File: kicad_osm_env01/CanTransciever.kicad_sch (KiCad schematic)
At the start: 21 parts

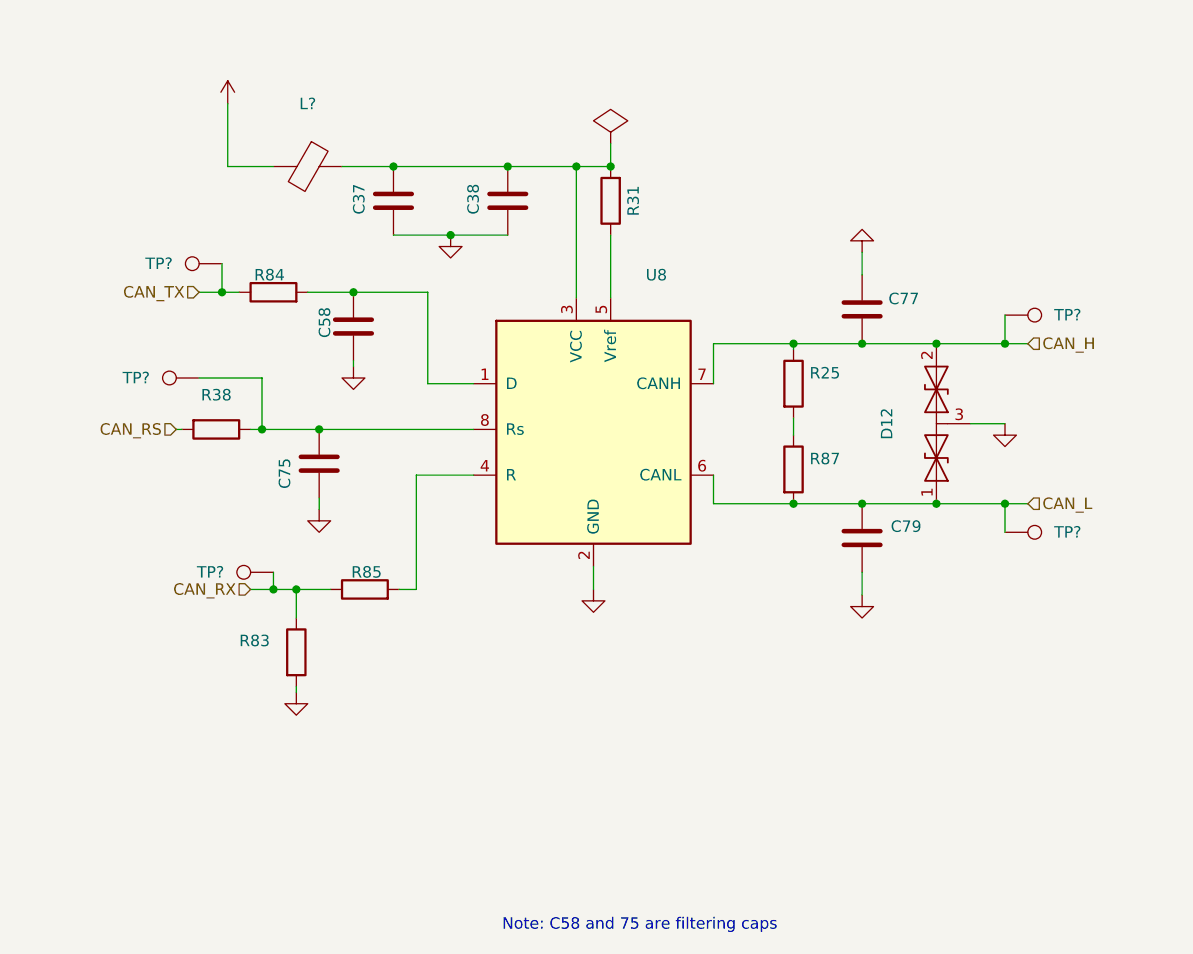
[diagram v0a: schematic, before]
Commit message: added stml433 to schematic and carried out some mods
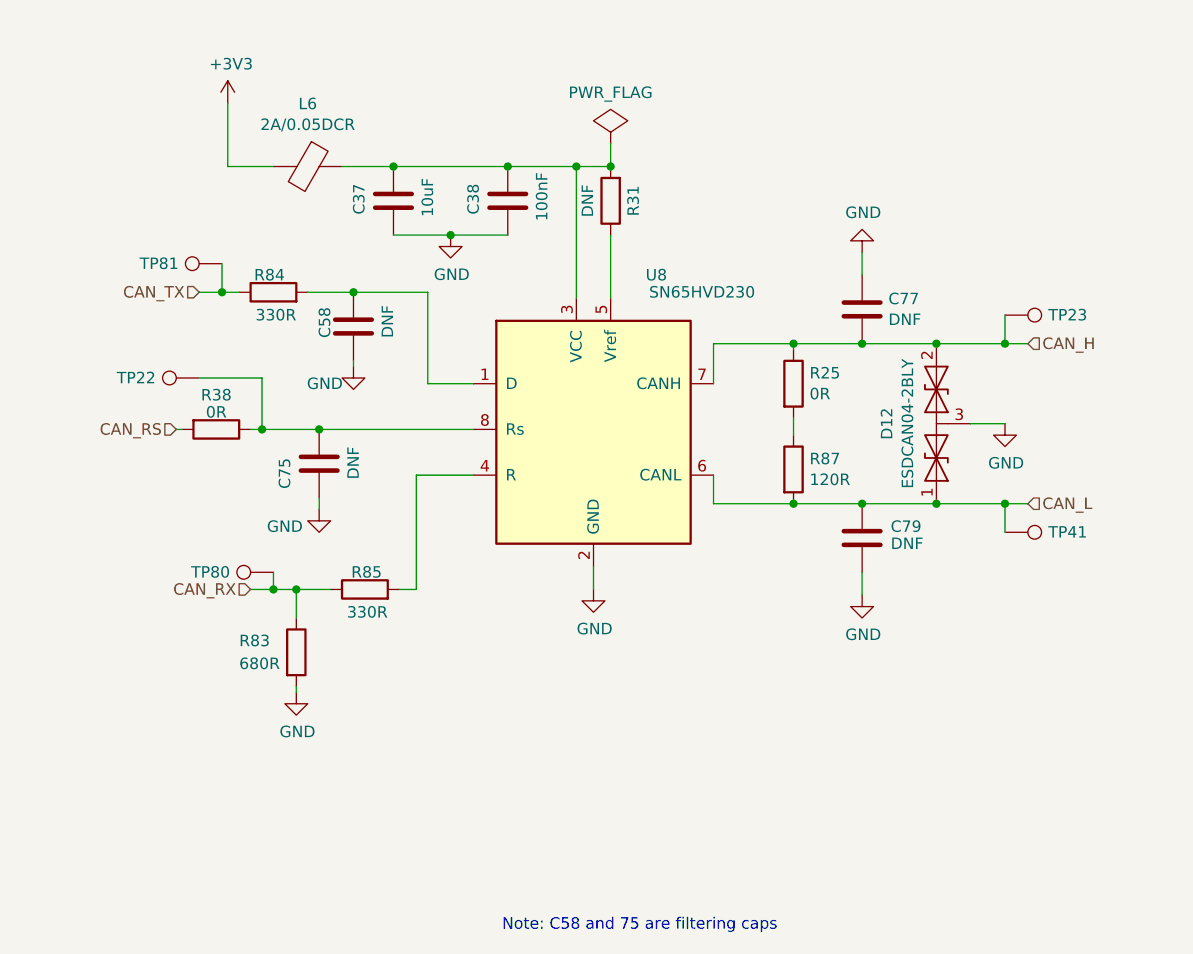
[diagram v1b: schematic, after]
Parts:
- C37: value (none) -> 10uF; footprint (none) -> Capacitor_SMD:C_0603_1608Metric
- C38: value (none) -> 100nF; footprint (none) -> Capacitor_SMD:C_0402_1005Metric
- C58, C75, C77, C79: value (none) -> DNF; footprint (none) -> Capacitor_SMD:C_0603_1608Metric
- D12: value (none) -> ESDCAN04-2BLY; footprint (none) -> Package_TO_SOT_SMD:SOT-23
- L6: renamed from L?; value (none) -> 2A/0.05DCR; footprint (none) -> Inductor_SMD:L_0402_1005Metric
- R25, R38: value (none) -> 0R; footprint (none) -> Resistor_SMD:R_0603_1608Metric
- R31: value (none) -> DNF; footprint (none) -> Resistor_SMD:R_0603_1608Metric
- R83: value (none) -> 680R; footprint (none) -> Resistor_SMD:R_0603_1608Metric
- R84, R85: value (none) -> 330R; footprint (none) -> Resistor_SMD:R_0603_1608Metric
- R87: value (none) -> 120R; footprint (none) -> Resistor_SMD:R_0603_1608Metric
- TP22, TP23, TP41, TP80, TP81: renamed from TP?; value (none) -> Test_Point; footprint (none) -> TestPoint:TestPoint_Pad_D1.5mm
- U8: value (none) -> SN65HVD230; footprint (none) -> Package_SO:SOIC-8_3.9x4.9mm_P1.27mm

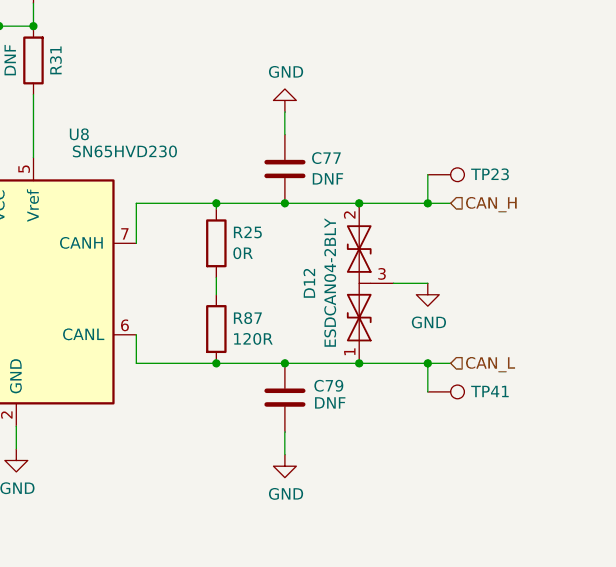
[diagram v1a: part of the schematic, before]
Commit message: updated mod list
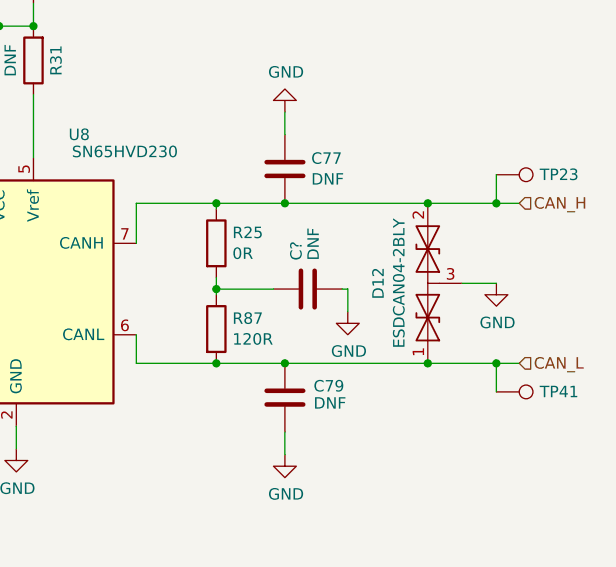
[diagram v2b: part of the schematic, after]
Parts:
- added C?: DNF, Capacitor_SMD:C_0603_1608Metric, symbol device:C
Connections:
- net GND: now also C?.1
- net at R25.2, R87.1: now also C?.2
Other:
- moved on the sheet: D12, TP23, TP41

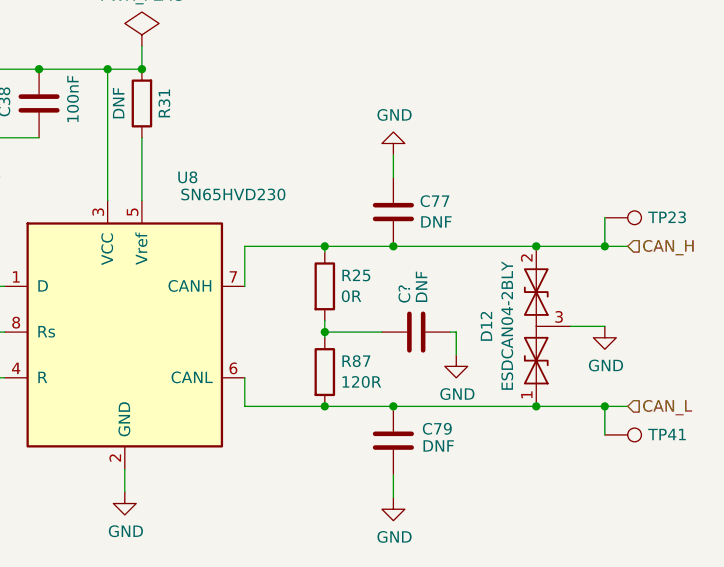
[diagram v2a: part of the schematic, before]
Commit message: added new battery charge ic u2
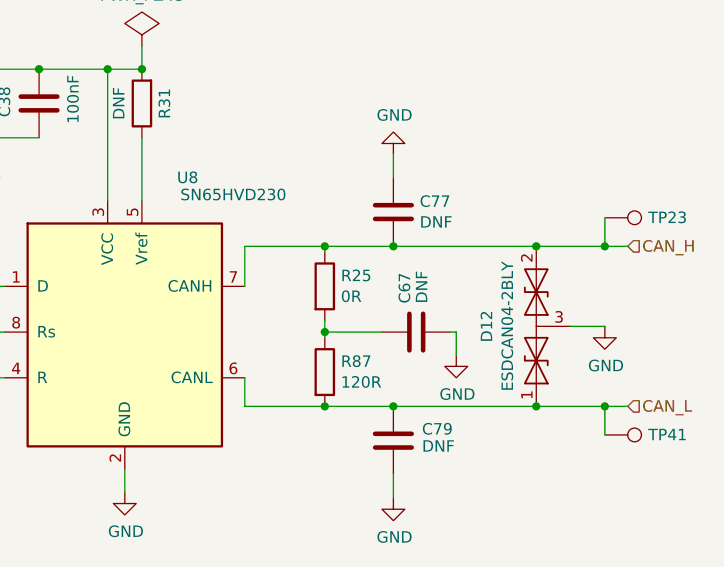
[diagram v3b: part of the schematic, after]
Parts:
- gave numbers to parts that had none: 1
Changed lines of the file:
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@@
   (title_block
     (title "Open Smart Monitor")
-    (date "2021-09-29")
-    (rev "B")
+    (date "2022-07-01")
+    (rev "C")
     (company "Devtank LTD")
     (comment 1 "Part No: 304-010")
@@
   (symbol (lib_id "device:C") (at 185.42 101.6 270) (mirror x) (unit 1)
     (in_bom yes) (on_board yes)
-    (property "Reference" "C?" (id 0) (at 184.15 98.425 0)
+    (property "Reference" "C67" (id 0) (at 184.15 98.425 0)
       (effects (font (size 1.27 1.27)) (justify left))
     )
@@
   (symbol (lib_id "OSM_env01:GND") (at 189.865 104.14 0) (unit 1)
     (in_bom yes) (on_board yes)
-    (property "Reference" "#PWR?" (id 0) (at 189.865 110.49 0)
-      (effects (font (size 1.27 1.27)) hide)
-    )
+    (property "Reference" "#PWR078" (id 0) (at 189.865 110.49 0)
+      (effects (font (size 1.27 1.27)) hide)
+    )

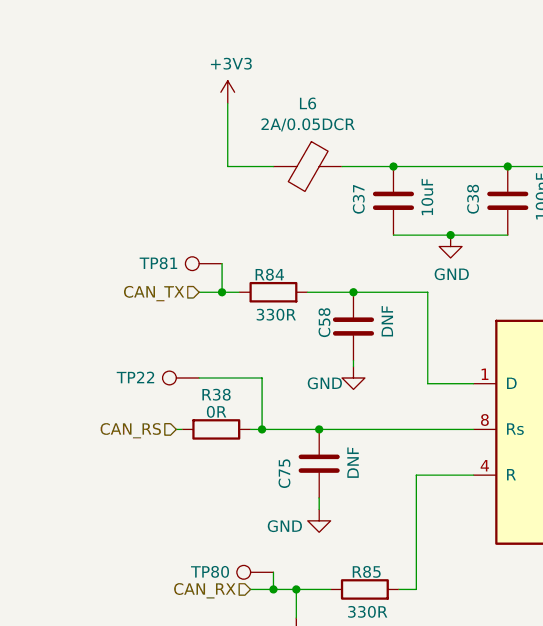
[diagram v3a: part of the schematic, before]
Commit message: Schematics waiting review
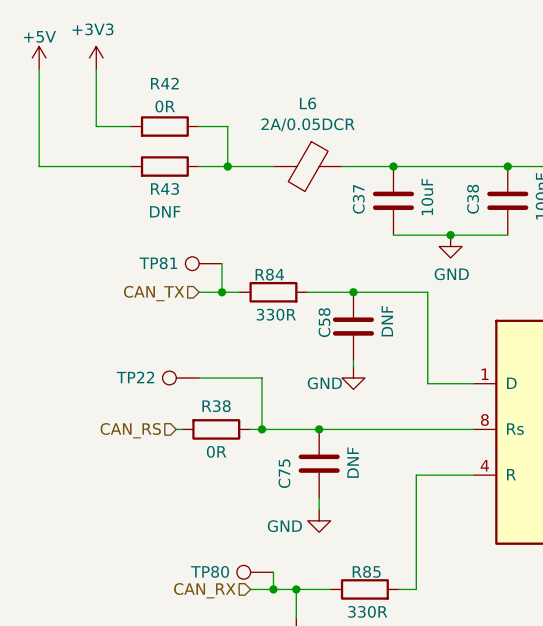
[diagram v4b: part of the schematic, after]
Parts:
- added R42: 0R, symbol device:R
- added R43: DNF, symbol device:R
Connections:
- net +3V3: now also R42.2; no longer L6.2
- new net: L6.2, R42.1, R43.1
- new net +5V: R43.2
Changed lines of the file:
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@@
   (junction (at 116.205 101.6) (diameter 0) (color 0 0 0 0)
   )
+  (junction (at 112.395 72.39) (diameter 0) (color 0 0 0 0)
+  )
   (junction (at 198.755 109.855) (diameter 0) (color 0 0 0 0)
   )
@@
     (stroke (width 0) (type default) (color 0 0 0 0))
   )
+  (wire (pts (xy 101.6 67.945) (xy 97.79 67.945))
+    (stroke (width 0) (type default) (color 0 0 0 0))
+  )
   (wire (pts (xy 134.62 86.36) (xy 126.365 86.36))
     (stroke (width 0) (type default) (color 0 0 0 0))
@@
     (stroke (width 0) (type default) (color 0 0 0 0))
   )
-  (wire (pts (xy 112.395 65.405) (xy 112.395 72.39))
-    (stroke (width 0) (type default) (color 0 0 0 0))
-  )
   (wire (pts (xy 182.88 109.855) (xy 175.26 109.855))
     (stroke (width 0) (type default) (color 0 0 0 0))
@@
     (stroke (width 0) (type default) (color 0 0 0 0))
   )
+  (wire (pts (xy 91.44 61.595) (xy 91.44 72.39))
+    (stroke (width 0) (type default) (color 0 0 0 0))
+  )
   (wire (pts (xy 133.35 106.68) (xy 139.7 106.68))
     (stroke (width 0) (type default) (color 0 0 0 0))
@@
     (stroke (width 0) (type default) (color 0 0 0 0))
   )
+  (wire (pts (xy 112.395 67.945) (xy 112.395 72.39))
+    (stroke (width 0) (type default) (color 0 0 0 0))
+  )
   (wire (pts (xy 189.865 101.6) (xy 189.865 104.14))
     (stroke (width 0) (type default) (color 0 0 0 0))
   )
+  (wire (pts (xy 112.395 67.945) (xy 109.22 67.945))
+    (stroke (width 0) (type default) (color 0 0 0 0))
+  )
+  (wire (pts (xy 109.22 72.39) (xy 112.395 72.39))
+    (stroke (width 0) (type default) (color 0 0 0 0))
+  )
   (wire (pts (xy 166.37 106.68) (xy 166.37 109.855))
     (stroke (width 0) (type default) (color 0 0 0 0))
   )
+  (wire (pts (xy 97.79 61.595) (xy 97.79 67.945))
+    (stroke (width 0) (type default) (color 0 0 0 0))
+  )
   (wire (pts (xy 114.935 119.38) (xy 117.475 119.38))
     (stroke (width 0) (type default) (color 0 0 0 0))
@@
   )
   (wire (pts (xy 182.88 84.455) (xy 182.88 81.915))
+    (stroke (width 0) (type default) (color 0 0 0 0))
+  )
+  (wire (pts (xy 101.6 72.39) (xy 91.44 72.39))
     (stroke (width 0) (type default) (color 0 0 0 0))
   )
@@
     (property "Datasheet" "" (id 3) (at 137.16 80.01 0)
       (effects (font (size 1.524 1.524)))
-    )
-    (pin "1")
-  )
-  (symbol (lib_id "power:+3V3") (at 112.395 65.405 0) (unit 1)
-    (in_bom yes) (on_board yes)
-    (property "Reference" "#PWR062" (id 0) (at 112.395 69.215 0)
-      (effects (font (size 1.27 1.27)) hide)
-    )
-    (property "Value" "+3V3" (id 1) (at 112.776 61.0108 0))
-    (property "Footprint" "" (id 2) (at 112.395 65.405 0)
-      (effects (font (size 1.27 1.27)) hide)
-    )
-    (property "Datasheet" "" (id 3) (at 112.395 65.405 0)
-      (effects (font (size 1.27 1.27)) hide)
     )
     (pin "1")
@@
   (symbol (lib_id "device:R") (at 111.125 101.6 270) (unit 1)
     (in_bom yes) (on_board yes)
-    (property "Reference" "R38" (id 0) (at 111.125 97.79 90))
-    (property "Value" "0R" (id 1) (at 111.125 99.695 90))
+    (property "Reference" "R38" (id 0) (at 111.125 99.06 90))
+    (property "Value" "0R" (id 1) (at 111.125 104.14 90))
     (property "Footprint" "Resistor_SMD:R_0603_1608Metric" (id 2) (at 111.125 99.822 90)
       (effects (font (size 1.27 1.27)) hide)
@@
     )
     (pin "1")
+  )
+  (symbol (lib_id "device:R") (at 105.41 67.945 270) (mirror x) (unit 1)
+    (in_bom yes) (on_board yes) (fields_autoplaced)
+    (property "Reference" "R42" (id 0) (at 105.41 63.2292 90))
+    (property "Value" "0R" (id 1) (at 105.41 65.7661 90))
+    (property "Footprint" "" (id 2) (at 105.41 69.723 90)
+      (effects (font (size 1.27 1.27)) hide)
+    )
+    (property "Datasheet" "" (id 3) (at 105.41 67.945 0)
+      (effects (font (size 1.27 1.27)) hide)
+    )
+    (pin "1")
+    (pin "2")
+  )
+  (symbol (lib_id "OSM_env01:+5V") (at 91.44 61.595 0) (mirror y) (unit 1)
+    (in_bom yes) (on_board yes) (fields_autoplaced)
+    (property "Reference" "#PWR010" (id 0) (at 91.44 65.405 0)
+      (effects (font (size 1.27 1.27)) hide)
+    )
+    (property "Value" "+5V" (id 1) (at 91.44 58.0192 0))
+    (property "Footprint" "" (id 2) (at 91.44 61.595 0)
+      (effects (font (size 1.524 1.524)))
+    )
+    (property "Datasheet" "" (id 3) (at 91.44 61.595 0)
+      (effects (font (size 1.524 1.524)))
+    )
+    (pin "1")
+  )
+  (symbol (lib_id "device:R") (at 105.41 72.39 270) (mirror x) (unit 1)
+    (in_bom yes) (on_board yes)
+    (property "Reference" "R43" (id 0) (at 105.41 74.93 90))
+    (property "Value" "DNF" (id 1) (at 105.41 77.47 90))
+    (property "Footprint" "" (id 2) (at 105.41 74.168 90)
+      (effects (font (size 1.27 1.27)) hide)
+    )
+    (property "Datasheet" "" (id 3) (at 105.41 72.39 0)
+      (effects (font (size 1.27 1.27)) hide)
+    )
+    (pin "1")
+    (pin "2")
+  )
+  (symbol (lib_id "power:+3V3") (at 97.79 61.595 0) (mirror y) (unit 1)
+    (in_bom yes) (on_board yes)
+    (property "Reference" "#PWR024" (id 0) (at 97.79 65.405 0)
+      (effects (font (size 1.27 1.27)) hide)
+    )
+    (property "Value" "+3V3" (id 1) (at 97.409 57.2008 0))
+    (property "Footprint" "" (id 2) (at 97.79 61.595 0)
+      (effects (font (size 1.27 1.27)) hide)
+    )
+    (property "Datasheet" "" (id 3) (at 97.79 61.595 0)
+      (effects (font (size 1.27 1.27)) hide)
+    )
+    (pin "1")

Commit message: started layout with throwdown
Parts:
- removed U8: SN65HVD230, Package_SO:SOIC-8_3.9x4.9mm_P1.27mm, symbol interface:SN65HVD230
- added U8: (no value), symbol Devtank:SN65HVD230
- C37: value 10uF -> (none); footprint Capacitor_SMD:C_0603_1608Metric -> (none); symbol device:C -> Device:C
- C38: value 100nF -> (none); footprint Capacitor_SMD:C_0402_1005Metric -> (none); symbol device:C -> Device:C
- C58, C67, C75, C77, C79: value DNF -> (none); footprint Capacitor_SMD:C_0603_1608Metric -> (none); symbol device:C -> Device:C
- D12: value ESDCAN04-2BLY -> (none); footprint Package_TO_SOT_SMD:SOT-23 -> (none); symbol device:D_TVS_x2_AAC -> Device:D_TVS_Dual_AAC
- L6: value 2A/0.05DCR -> (none); footprint Inductor_SMD:L_0402_1005Metric -> (none); symbol device:Ferrite_Bead -> Device:FerriteBead
- R25, R38: value 0R -> (none); footprint Resistor_SMD:R_0603_1608Metric -> (none); symbol device:R -> Device:R
- R31: value DNF -> (none); footprint Resistor_SMD:R_0603_1608Metric -> (none); symbol device:R -> Device:R
- R42: value 0R -> (none); symbol device:R -> Device:R
- R43: value DNF -> (none); symbol device:R -> Device:R
- R83: value 680R -> (none); footprint Resistor_SMD:R_0603_1608Metric -> (none); symbol device:R -> Device:R
- R84, R85: value 330R -> (none); footprint Resistor_SMD:R_0603_1608Metric -> (none); symbol device:R -> Device:R
- R87: value 120R -> (none); footprint Resistor_SMD:R_0603_1608Metric -> (none); symbol device:R -> Device:R
- TP22, TP23, TP41, TP80, TP81: value Test_Point -> (none); footprint TestPoint:TestPoint_Pad_D1.5mm -> (none)
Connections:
- net CAN_H: now also U8.7 (CANH)
- net CAN_L: now also U8.6 (CANL)
- net GND: now also U8.2 (VSS)
- net at C58.1, R84.2: now also U8.1 (D)
- net at R85.2: now also U8.4 (R)
- net at C37.2, C38.2, L6.1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: now also U8.3 (VCC)
- net at R31.1: now also U8.5 (Vref)
- net at C75.2, R38.1, TP22.1: now also U8.8 (Rs)
